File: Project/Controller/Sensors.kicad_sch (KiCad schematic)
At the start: 10 parts, among them J4 Bar30, U7 BMI088, U8 MMC5983MA, U9 MCP9700Ax-ETT

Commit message: Change 0402 footprints to 0603
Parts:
- C20, C21, C22, C32: footprint Capacitor_SMD:C_0402_1005Metric -> Capacitor_SMD:C_0603_1608Metric; Listing https://www.digikey.com/en/products/detail/samsung-electro-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 -> https://www.digikey.com/en/products/detail/yageo/CC0603KRX7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
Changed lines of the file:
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@@
 			)
 		)
-		(property "Footprint" "Capacitor_SMD:C_0402_1005Metric"
+		(property "Footprint" "Capacitor_SMD:C_0603_1608Metric"
 			(at 242.2652 111.76 0)
 			(effects
@@
 			)
 		)
-		(property "Datasheet" "https://mm.digikey.com/Volume0/opasdata/d220001/medias/docus/503/CL05A104KA5NNNC.pdf"
+		(property "Datasheet" "https://yageogroup.com/download/specsheet/CC0603KRX7R7BB104"
 			(at 241.3 107.95 0)
 			(effects
@@
 			)
 		)
-		(property "Listing" "https://www.digikey.com/en/products/detail/samsung-electro-mechanics/CL05A104KA5NNNC/3886701"
+		(property "Listing" "https://www.digikey.com/en/products/detail/yageo/CC0603KRX7R7BB104/302822"
 			(at 241.3 107.95 0)
 			(effects
@@
 			)
 		)
-		(property "Footprint" "Capacitor_SMD:C_0402_1005Metric"
+		(property "Footprint" "Capacitor_SMD:C_0603_1608Metric"
 			(at 127.9652 54.61 0)
 			(effects
@@
 			)
 		)
-		(property "Datasheet" "https://mm.digikey.com/Volume0/opasdata/d220001/medias/docus/503/CL05A104KA5NNNC.pdf"
+		(property "Datasheet" "https://yageogroup.com/download/specsheet/CC0603KRX7R7BB104"
 			(at 127 50.8 0)
 			(effects
@@
 			)
 		)
-		(property "Listing" "https://www.digikey.com/en/products/detail/samsung-electro-mechanics/CL05A104KA5NNNC/3886701"
+		(property "Listing" "https://www.digikey.com/en/products/detail/yageo/CC0603KRX7R7BB104/302822"
 			(at 127 50.8 0)
 			(effects
@@
 			)
 		)
-		(property "Footprint" "Capacitor_SMD:C_0402_1005Metric"
+		(property "Footprint" "Capacitor_SMD:C_0603_1608Metric"
 			(at 229.5652 54.61 0)
 			(effects
@@
 			)
 		)
-		(property "Datasheet" "https://mm.digikey.com/Volume0/opasdata/d220001/medias/docus/503/CL05A104KA5NNNC.pdf"
+		(property "Datasheet" "https://yageogroup.com/download/specsheet/CC0603KRX7R7BB104"
 			(at 228.6 50.8 0)
 			(effects
@@
 			)
 		)
-		(property "Listing" "https://www.digikey.com/en/products/detail/samsung-electro-mechanics/CL05A104KA5NNNC/3886701"
+		(property "Listing" "https://www.digikey.com/en/products/detail/yageo/CC0603KRX7R7BB104/302822"
 			(at 228.6 50.8 0)
 			(effects
@@
 			)
 		)
-		(property "Footprint" "Capacitor_SMD:C_0402_1005Metric"
+		(property "Footprint" "Capacitor_SMD:C_0603_1608Metric"
 			(at 140.6652 54.61 0)
 			(effects
@@
 			)
 		)
-		(property "Datasheet" "https://mm.digikey.com/Volume0/opasdata/d220001/medias/docus/503/CL05A104KA5NNNC.pdf"
+		(property "Datasheet" "https://yageogroup.com/download/specsheet/CC0603KRX7R7BB104"
 			(at 139.7 50.8 0)
 			(effects
@@
 			)
 		)
-		(property "Listing" "https://www.digikey.com/en/products/detail/samsung-electro-mechanics/CL05A104KA5NNNC/3886701"
+		(property "Listing" "https://www.digikey.com/en/products/detail/yageo/CC0603KRX7R7BB104/302822"
 			(at 139.7 50.8 0)
 			(effects

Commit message: Re-annotate symbols
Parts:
- renumbered C20 to C21, C21 to C22, C22 to C23, C32 to C24, C23 to C25, C24 to C26
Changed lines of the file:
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@@
 		(dnp no)
 		(fields_autoplaced yes)
-		(property "Reference" "#PWR099"
+		(property "Reference" "#PWR061"
 			(at 241.3 120.65 0)
 			(effects
@@
 			(project "XuLabController"
 				(path "/71bb14ae-b730-4d22-a41d-cf68989dae2d/a5713b00-422c-456a-9938-13721b057665"
-					(reference "#PWR099")
+					(reference "#PWR061")
 					(unit 1)
 				)
@@
 		(dnp no)
 		(fields_autoplaced yes)
-		(property "Reference" "#PWR050"
+		(property "Reference" "#PWR059"
 			(at 147.32 107.95 0)
 			(effects
@@
 			(project "XuLabController"
 				(path "/71bb14ae-b730-4d22-a41d-cf68989dae2d/a5713b00-422c-456a-9938-13721b057665"
-					(reference "#PWR050")
+					(reference "#PWR059")
 					(unit 1)
 				)
@@
 		(dnp no)
 		(fields_autoplaced yes)
-		(property "Reference" "#PWR046"
+		(property "Reference" "#PWR048"
 			(at 228.6 48.26 0)
 			(effects
@@
 			(project "XuLabController"
 				(path "/71bb14ae-b730-4d22-a41d-cf68989dae2d/a5713b00-422c-456a-9938-13721b057665"
-					(reference "#PWR046")
+					(reference "#PWR048")
 					(unit 1)
 				)
@@
 		(dnp no)
 		(fields_autoplaced yes)
-		(property "Reference" "#PWR042"
+		(property "Reference" "#PWR052"
 			(at 139.7 63.5 0)
 			(effects
@@
 			(project "XuLabController"
 				(path "/71bb14ae-b730-4d22-a41d-cf68989dae2d/a5713b00-422c-456a-9938-13721b057665"
-					(reference "#PWR042")
+					(reference "#PWR052")
 					(unit 1)
 				)
@@
 		(dnp no)
 		(fields_autoplaced yes)
-		(property "Reference" "C32"
+		(property "Reference" "C24"
 			(at 245.11 106.6799 0)
 			(effects
@@
 			(project "XuLabController"
 				(path "/71bb14ae-b730-4d22-a41d-cf68989dae2d/a5713b00-422c-456a-9938-13721b057665"
-					(reference "C32")
+					(reference "C24")
 					(unit 1)
 				)
@@
 		(dnp no)
 		(fields_autoplaced yes)
-		(property "Reference" "#PWR098"
+		(property "Reference" "#PWR058"
 			(at 241.3 105.41 0)
 			(effects
@@
 			(project "XuLabController"
 				(path "/71bb14ae-b730-4d22-a41d-cf68989dae2d/a5713b00-422c-456a-9938-13721b057665"
-					(reference "#PWR098")
+					(reference "#PWR058")
 					(unit 1)
 				)
@@
 		(dnp no)
 		(fields_autoplaced yes)
-		(property "Reference" "#PWR039"
+		(property "Reference" "#PWR046"
 			(at 127 48.26 0)
 			(effects
@@
 			(project "XuLabController"
 				(path "/71bb14ae-b730-4d22-a41d-cf68989dae2d/a5713b00-422c-456a-9938-13721b057665"
-					(reference "#PWR039")
+					(reference "#PWR046")
 					(unit 1)
 				)
@@
 		(dnp no)
 		(fields_autoplaced yes)
-		(property "Reference" "C23"
+		(property "Reference" "C25"
 			(at 151.13 109.2199 0)
 			(effects
@@
 			(project "XuLabController"
 				(path "/71bb14ae-b730-4d22-a41d-cf68989dae2d/a5713b00-422c-456a-9938-13721b057665"
-					(reference "C23")
+					(reference "C25")
 					(unit 1)
 				)
@@
 		(dnp no)
 		(fields_autoplaced yes)
-		(property "Reference" "#PWR048"
+		(property "Reference" "#PWR053"
 			(at 228.6 63.5 0)
 			(effects
@@
 			(project "XuLabController"
 				(path "/71bb14ae-b730-4d22-a41d-cf68989dae2d/a5713b00-422c-456a-9938-13721b057665"
-					(reference "#PWR048")
+					(reference "#PWR053")
 					(unit 1)
 				)
@@
 		(dnp no)
 		(fields_autoplaced yes)
-		(property "Reference" "#PWR049"
+		(property "Reference" "#PWR057"
 			(at 54.61 101.6 0)
 			(effects
@@
 			(project "XuLabController"
 				(path "/71bb14ae-b730-4d22-a41d-cf68989dae2d/a5713b00-422c-456a-9938-13721b057665"
-					(reference "#PWR049")
+					(reference "#PWR057")
 					(unit 1)
 				)
@@
 		(dnp no)
 		(fields_autoplaced yes)
-		(property "Reference" "#PWR040"
+		(property "Reference" "#PWR047"
 			(at 139.7 48.26 0)
 			(effects
@@
 			(project "XuLabController"
 				(path "/71bb14ae-b730-4d22-a41d-cf68989dae2d/a5713b00-422c-456a-9938-13721b057665"
-					(reference "#PWR040")
+					(reference "#PWR047")
 					(unit 1)
 				)
@@
 		(dnp no)
 		(fields_autoplaced yes)
-		(property "Reference" "#PWR097"
+		(property "Reference" "#PWR063"
 			(at 203.2 124.46 0)
 			(effects
@@
 			(project "XuLabController"
 				(path "/71bb14ae-b730-4d22-a41d-cf68989dae2d/a5713b00-422c-456a-9938-13721b057665"
-					(reference "#PWR097")
+					(reference "#PWR063")
 					(unit 1)
 				)
@@
 		(dnp no)
 		(fields_autoplaced yes)
-		(property "Reference" "#PWR053"
+		(property "Reference" "#PWR064"
 			(at 124.46 129.54 0)
 			(effects
@@
 			(project "XuLabController"
 				(path "/71bb14ae-b730-4d22-a41d-cf68989dae2d/a5713b00-422c-456a-9938-13721b057665"
-					(reference "#PWR053")
+					(reference "#PWR064")
 					(unit 1)
 				)
@@
 		(dnp no)
 		(fields_autoplaced yes)
-		(property "Reference" "#PWR096"
+		(property "Reference" "#PWR056"
 			(at 203.2 101.6 0)
 			(effects
@@
 			(project "XuLabController"
 				(path "/71bb14ae-b730-4d22-a41d-cf68989dae2d/a5713b00-422c-456a-9938-13721b057665"
-					(reference "#PWR096")
+					(reference "#PWR056")
 					(unit 1)
 				)
@@
 		(dnp no)
 		(fields_autoplaced yes)
-		(property "Reference" "C20"
+		(property "Reference" "C21"
 			(at 130.81 49.5299 0)
 			(effects
@@
 			(project "XuLabController"
 				(path "/71bb14ae-b730-4d22-a41d-cf68989dae2d/a5713b00-422c-456a-9938-13721b057665"
-					(reference "C20")
+					(reference "C21")
 					(unit 1)
 				)
@@
 		(on_board yes)
 		(dnp no)
-		(property "Reference" "#PWR047"
+		(property "Reference" "#PWR050"
 			(at 198.12 62.23 0)
 			(effects
@@
 			(project "XuLabController"
 				(path "/71bb14ae-b730-4d22-a41d-cf68989dae2d/a5713b00-422c-456a-9938-13721b057665"
-					(reference "#PWR047")
+					(reference "#PWR050")
 					(unit 1)
 				)
@@
 		(dnp no)
 		(fields_autoplaced yes)
-		(property "Reference" "#PWR045"
+		(property "Reference" "#PWR049"
 			(at 198.12 49.53 0)
 			(effects
@@
 			(project "XuLabController"
 				(path "/71bb14ae-b730-4d22-a41d-cf68989dae2d/a5713b00-422c-456a-9938-13721b057665"
-					(reference "#PWR045")
+					(reference "#PWR049")
 					(unit 1)
 				)
@@
 		(dnp no)
 		(fields_autoplaced yes)
-		(property "Reference" "C22"
+		(property "Reference" "C23"
 			(at 232.41 49.5299 0)
 			(effects
@@
 			(project "XuLabController"
 				(path "/71bb14ae-b730-4d22-a41d-cf68989dae2d/a5713b00-422c-456a-9938-13721b057665"
-					(reference "C22")
+					(reference "C23")
 					(unit 1)
 				)
@@
 		(dnp no)
 		(fields_autoplaced yes)
-		(property "Reference" "C24"
+		(property "Reference" "C26"
 			(at 133.35 116.8399 0)
 			(effects
@@
 			(project "XuLabController"
 				(path "/71bb14ae-b730-4d22-a41d-cf68989dae2d/a5713b00-422c-456a-9938-13721b057665"
-					(reference "C24")
+					(reference "C26")
 					(unit 1)
 				)
@@
 		(dnp no)
 		(fields_autoplaced yes)
-		(property "Reference" "#PWR044"
+		(property "Reference" "#PWR055"
 			(at 86.36 74.93 0)
 			(effects
@@
 			(project "XuLabController"
 				(path "/71bb14ae-b730-4d22-a41d-cf68989dae2d/a5713b00-422c-456a-9938-13721b057665"
-					(reference "#PWR044")
+					(reference "#PWR055")
 					(unit 1)
 				)
@@
 		(dnp no)
 		(fields_autoplaced yes)
-		(property "Reference" "#PWR038"
+		(property "Reference" "#PWR045"
 			(at 86.36 35.56 0)
 			(effects
@@
 			(project "XuLabController"
 				(path "/71bb14ae-b730-4d22-a41d-cf68989dae2d/a5713b00-422c-456a-9938-13721b057665"
-					(reference "#PWR038")
+					(reference "#PWR045")
 					(unit 1)
 				)
@@
 		(dnp no)
 		(fields_autoplaced yes)
-		(property "Reference" "#PWR052"
+		(property "Reference" "#PWR062"
 			(at 147.32 123.19 0)
 			(effects
@@
 			(project "XuLabController"
 				(path "/71bb14ae-b730-4d22-a41d-cf68989dae2d/a5713b00-422c-456a-9938-13721b057665"
-					(reference "#PWR052")
+					(reference "#PWR062")
 					(unit 1)
 				)
@@
 		(dnp no)
 		(fields_autoplaced yes)
-		(property "Reference" "C21"
+		(property "Reference" "C22"
 			(at 143.51 49.5299 0)
 			(effects
@@
 			(project "XuLabController"
 				(path "/71bb14ae-b730-4d22-a41d-cf68989dae2d/a5713b00-422c-456a-9938-13721b057665"
-					(reference "C21")
+					(reference "C22")
 					(unit 1)
 				)
@@
 		(dnp no)
 		(fields_autoplaced yes)
-		(property "Reference" "#PWR041"
+		(property "Reference" "#PWR051"
 			(at 127 63.5 0)
 			(effects
@@
 			(project "XuLabController"
 				(path "/71bb14ae-b730-4d22-a41d-cf68989dae2d/a5713b00-422c-456a-9938-13721b057665"
-					(reference "#PWR041")
+					(reference "#PWR051")
 					(unit 1)
 				)
@@
 		(dnp no)
 		(fields_autoplaced yes)
-		(property "Reference" "#PWR043"
+		(property "Reference" "#PWR054"
 			(at 74.93 69.85 0)
 			(effects
@@
 			(project "XuLabController"
 				(path "/71bb14ae-b730-4d22-a41d-cf68989dae2d/a5713b00-422c-456a-9938-13721b057665"
-					(reference "#PWR043")
+					(reference "#PWR054")
 					(unit 1)
 				)
@@
 		(dnp no)
 		(fields_autoplaced yes)
-		(property "Reference" "#PWR051"
+		(property "Reference" "#PWR060"
 			(at 123.19 106.68 0)
 			(effects
@@
 			(project "XuLabController"
 				(path "/71bb14ae-b730-4d22-a41d-cf68989dae2d/a5713b00-422c-456a-9938-13721b057665"
-					(reference "#PWR051")
-					(unit 1)
-				)
+					(reference "#PWR060")
+					(unit 1)
+				)

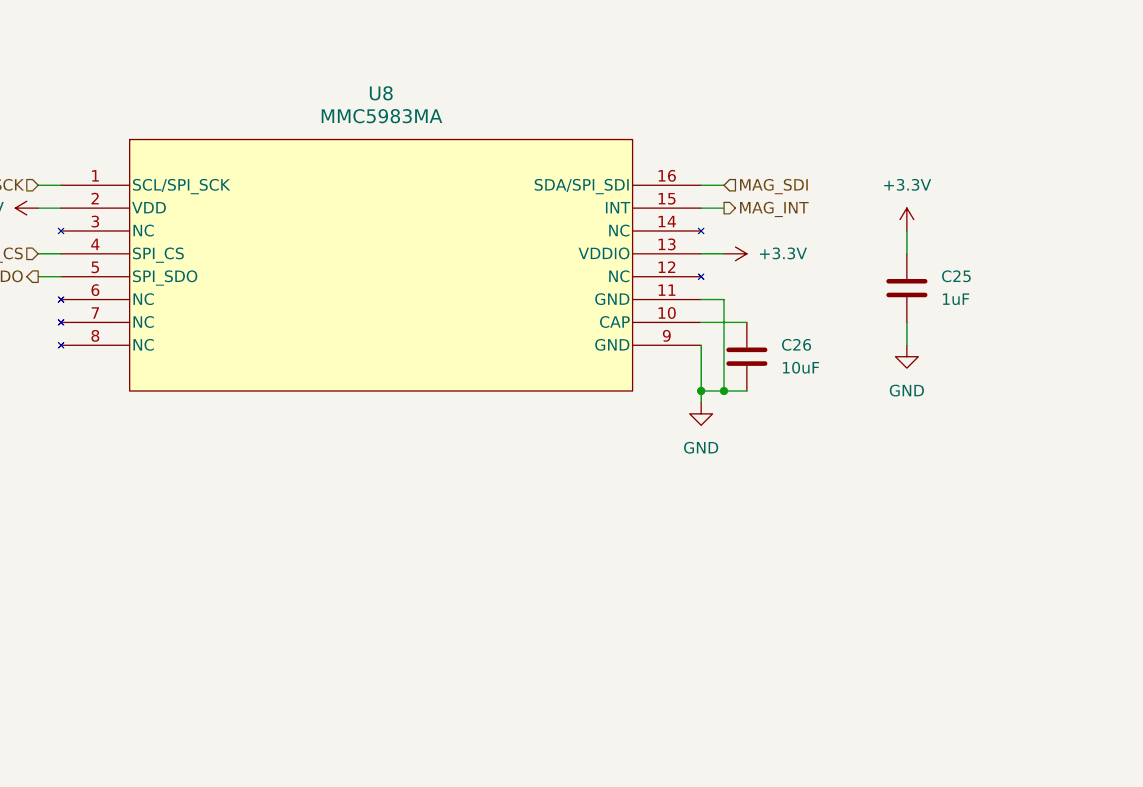
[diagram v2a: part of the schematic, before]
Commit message: Add SHTC3 humidity sensor
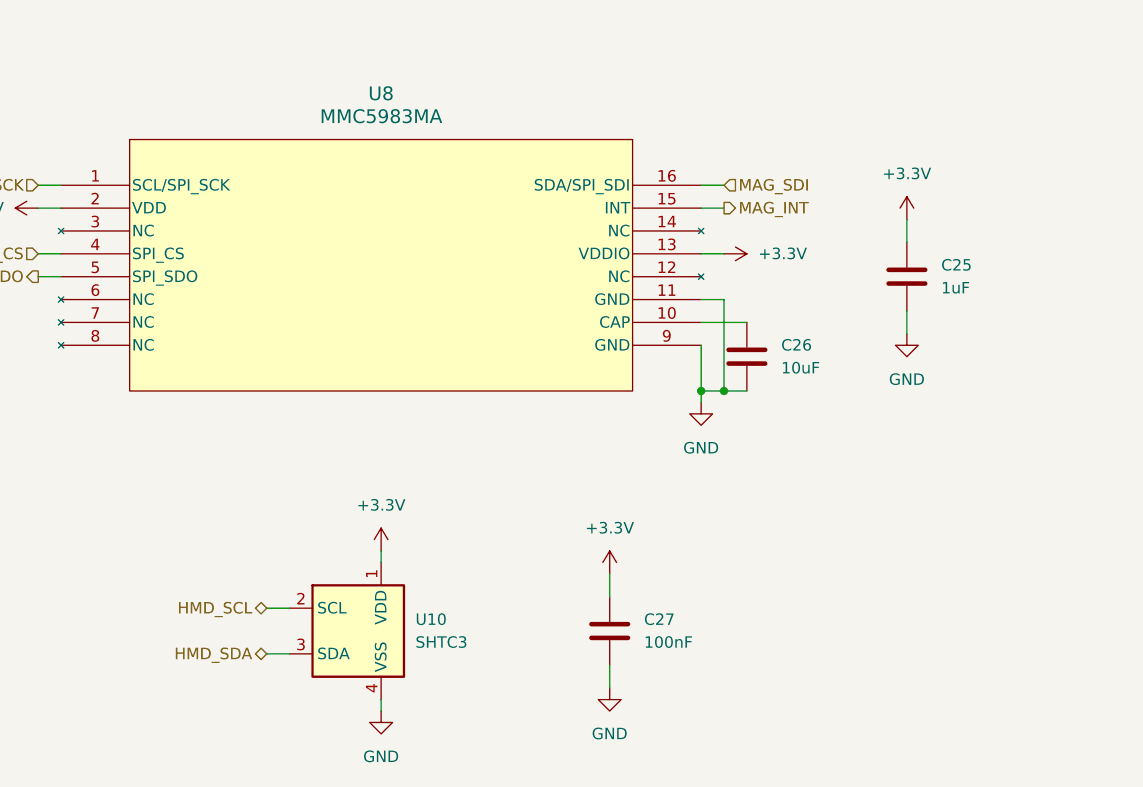
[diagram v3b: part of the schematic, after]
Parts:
- added C27: 100nF, Capacitor_SMD:C_0603_1608Metric, symbol Device:C
- added U10: SHTC3, Sensor_Humidity:Sensirion_DFN-4-1EP_2x2mm_P1mm_EP0.7x1.6mm, symbol Sensor_Humidity:SHTC3
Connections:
- net +3.3V: now also C27.1, U10.1 (VDD)
- net GND: now also C27.2, U10.4 (VSS)
- new net HMD_SCL: U10.2 (SCL)
- new net HMD_SDA: U10.3 (SDA)
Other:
- moved on the sheet: C25

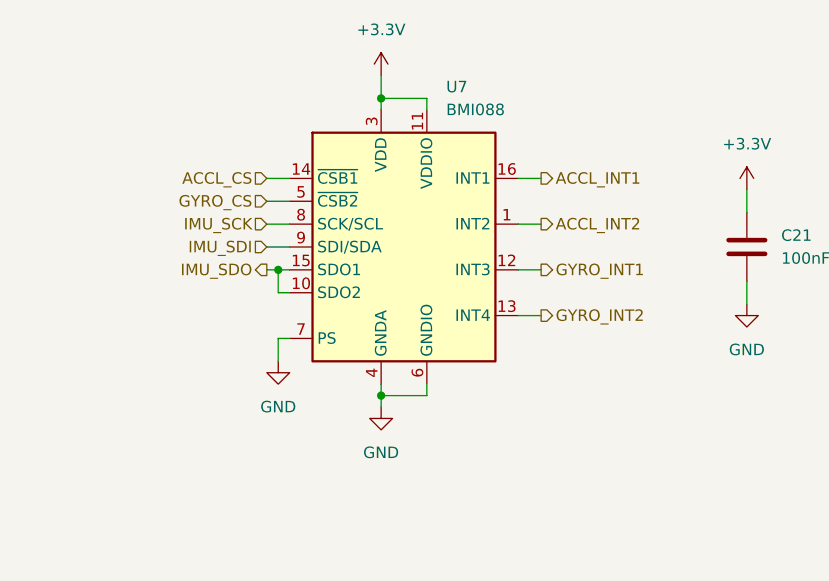
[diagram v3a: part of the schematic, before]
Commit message: Change IMU to BMI330
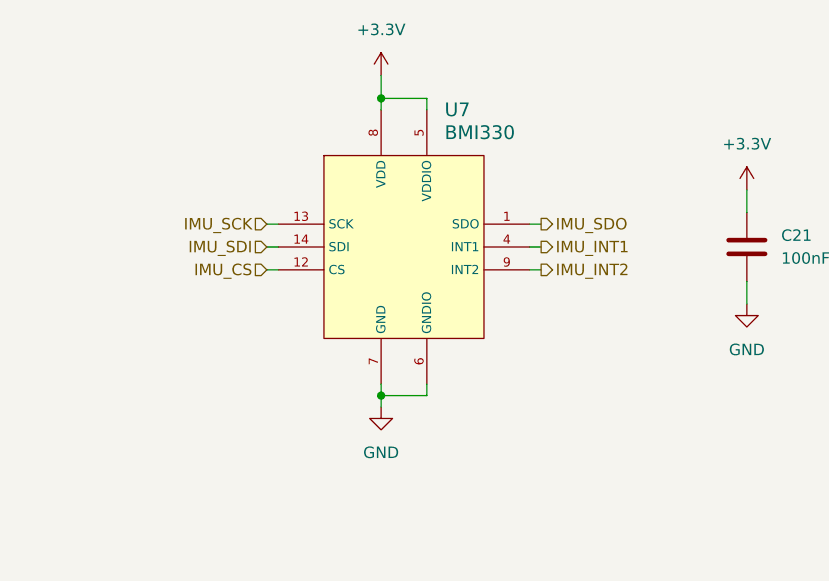
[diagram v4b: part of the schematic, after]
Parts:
- removed U7: BMI088, Package_LGA:Bosch_LGA-16_4.5x3mm_P0.5mm_LayoutBorder7x1y_ClockwisePinNumbering, symbol Sensor_Motion:BMI088
- added U7: BMI330, XuLab:BMI330, symbol XuLab:BMI330
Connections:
- net +3.3V: now also U7.5 (VDDIO), U7.8 (VDD)
- net GND: now also U7.6 (GNDIO), U7.7 (GND)
- net IMU_SCK: now also U7.13 (SCK)
- net IMU_SDI: now also U7.14 (SDI)
- net IMU_SDO: now also U7.1 (SDO)
- new net: U7.10 (NC), U7.11 (NC), U7.2 (NC), U7.3 (NC)
- new net IMU_CS: U7.12 (CS)
- new net IMU_INT1: U7.4 (INT1)
- new net IMU_INT2: U7.9 (INT2)
